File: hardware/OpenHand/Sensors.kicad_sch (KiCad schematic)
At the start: 56 parts, among them U5 LM324, U6 LM324

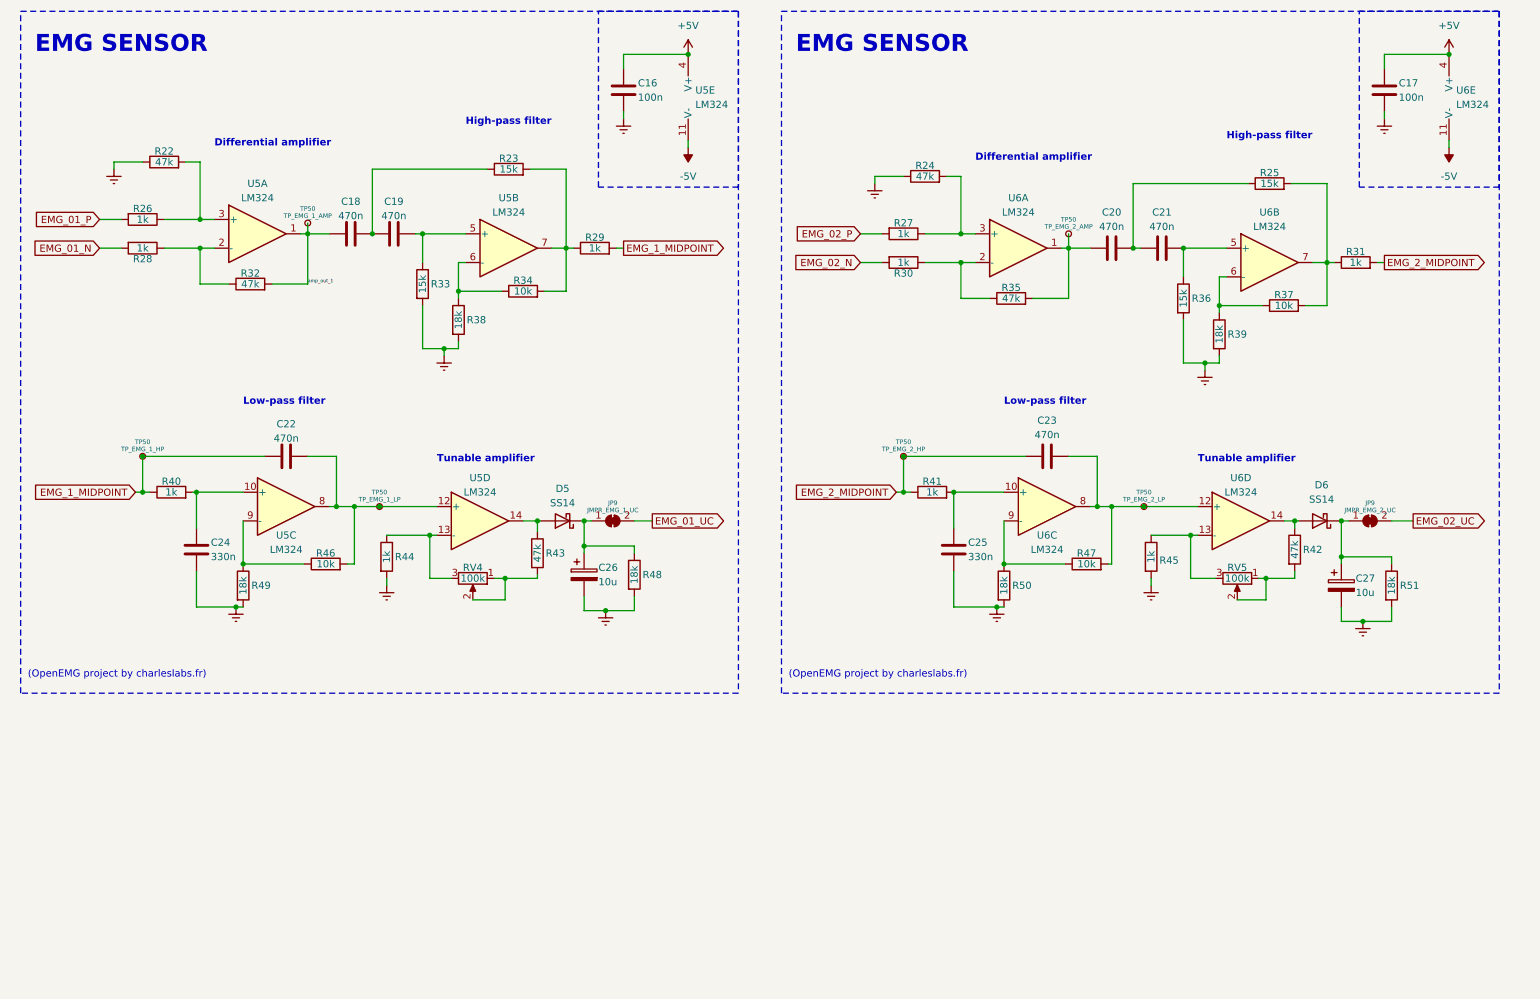
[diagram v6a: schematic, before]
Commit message: Update to KiCAD 8 and order components from LCSC
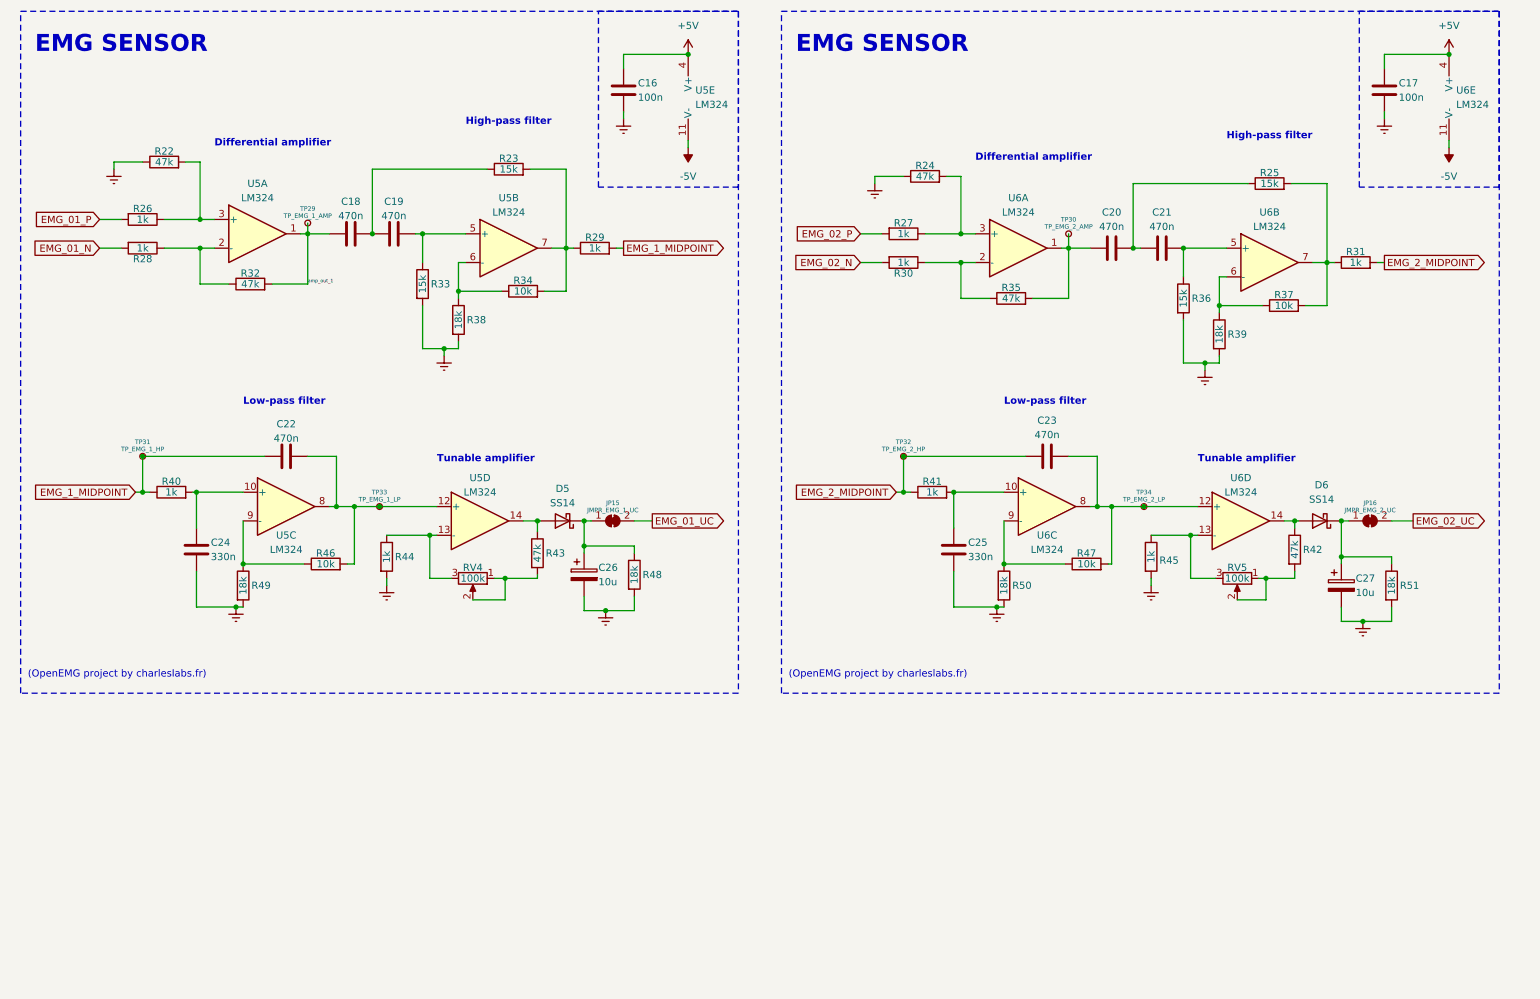
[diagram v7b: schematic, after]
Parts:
- renumbered JP9 to JP15, JP9 to JP16, TP50 to TP29, TP50 to TP30, TP50 to TP31, TP50 to TP32, TP50 to TP33, TP50 to TP34
